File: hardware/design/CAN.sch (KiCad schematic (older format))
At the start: 3 parts, among them IC1 MAX3051EKA+T

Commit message: Six-phase power stage.
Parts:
- renumbered C401 to Ccan1, R401 to Rcan1
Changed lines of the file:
@@
 $Descr A4 11693 8268
 encoding utf-8
-Sheet 2 6
+Sheet 2 12
 Title "CAN BUS transceiver"
 Date "2015-08-27"
@@
 $EndDescr
 $Comp
-L C-RESCUE-BLDC_4 C401
+L C-RESCUE-BLDC_4 Ccan1
 U 1 1 53F59FA3
 P 6950 2850
-F 0 "C401" H 7065 2889 40  0000 L CNN
+F 0 "Ccan1" H 7065 2889 40  0000 L CNN
 F 1 "2.2u" H 7065 2811 40  0000 L CNN
 F 2 "Capacitors_SMD:C_0603" H 6988 2700 30  0001 C CNN
@@
 CAN_TX
 $Comp
-L R-RESCUE-BLDC_4 R401
+L R-RESCUE-BLDC_4 Rcan1
 U 1 1 540030A8
 P 5250 3650
-F 0 "R401" V 5330 3650 40  0000 C CNN
-F 1 "NI" V 5257 3651 40  0000 C CNN
+F 0 "Rcan1" H 5321 3689 40  0000 L CNN
+F 1 "NI" H 5321 3611 40  0000 L CNN
 F 2 "Resistors_SMD:R_0603_HandSoldering" V 5180 3650 30  0001 C CNN
 F 3 "" H 5250 3650 30  0000 C CNN

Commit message: Some more routing...
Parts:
- removed IC1: MAX3051EKA+T, Housings_SOT_User:SOT-23-8, symbol MAX3051EKA+T
- added Ccan2: 2.2u, Capacitors_SMD:C_0603, symbol C
- added U2: ISO1050, CRF1:PDSO-G8, symbol ISO1050
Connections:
- net labels added: GND2, VCC2
- wire segments 12 -> 18
- no-connect marks 1 -> 0
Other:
- moved on the sheet: Ccan1, Rcan1
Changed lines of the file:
@@
 L C-RESCUE-BLDC_4 Ccan1
 U 1 1 53F59FA3
-P 6950 2850
-F 0 "Ccan1" H 7065 2889 40  0000 L CNN
-F 1 "2.2u" H 7065 2811 40  0000 L CNN
-F 2 "Capacitors_SMD:C_0603" H 6988 2700 30  0001 C CNN
-F 3 "" H 6950 2850 60  0000 C CNN
-	1    6950 2850
+P 9550 3250
+F 0 "Ccan1" H 9665 3289 40  0000 L CNN
+F 1 "2.2u" H 9665 3211 40  0000 L CNN
+F 2 "Capacitors_SMD:C_0603" H 9588 3100 30  0001 C CNN
+F 3 "" H 9550 3250 60  0000 C CNN
+	1    9550 3250
 	1    0    0    -1
 $EndComp
@@
 EndData
 $EndBitmap
-Text HLabel 6700 3450 2    60   Output ~ 0
+Text HLabel 8750 3200 2    60   Output ~ 0
 CAN_RX
-Text HLabel 6700 3550 2    60   Input ~ 0
+Text HLabel 8750 3300 2    60   Input ~ 0
 CAN_TX
 $Comp
 L R-RESCUE-BLDC_4 Rcan1
 U 1 1 540030A8
-P 5250 3650
-F 0 "Rcan1" H 5321 3689 40  0000 L CNN
-F 1 "NI" H 5321 3611 40  0000 L CNN
-F 2 "Resistors_SMD:R_0603_HandSoldering" V 5180 3650 30  0001 C CNN
-F 3 "" H 5250 3650 30  0000 C CNN
-	1    5250 3650
+P 7000 3250
+F 0 "Rcan1" H 7071 3289 40  0000 L CNN
+F 1 "NI" H 7071 3211 40  0000 L CNN
+F 2 "Resistors_SMD:R_0603_HandSoldering" V 6930 3250 30  0001 C CNN
+F 3 "" H 7000 3250 30  0000 C CNN
+	1    7000 3250
 	1    0    0    -1
 $EndComp
-Text HLabel 5000 3400 0    60   Input ~ 0
+Text HLabel 6650 3000 0    60   BiDi ~ 0
 CANH
-Text HLabel 5000 3900 0    60   Input ~ 0
+Text HLabel 6650 3500 0    60   BiDi ~ 0
 CANL
-Wire Wire Line
-	5500 3900 5000 3900
-Connection ~ 5250 3900
-Wire Wire Line
-	5500 3400 5000 3400
-Connection ~ 5250 3400
 Text Notes 3450 2000 0    60   ~ 0
 TODO: Bus protection
 $Comp
-L GND #PWR13
+L GND #PWR013
 U 1 1 55E64902
-P 6250 4200
-F 0 "#PWR13" H 6250 3950 50  0001 C CNN
-F 1 "GND" H 6250 4050 50  0000 C CNN
-F 2 "" H 6250 4200 60  0000 C CNN
-F 3 "" H 6250 4200 60  0000 C CNN
-	1    6250 4200
+P 9050 3650
+F 0 "#PWR013" H 9050 3400 50  0001 C CNN
+F 1 "GND" H 9050 3500 50  0000 C CNN
+F 2 "" H 9050 3650 60  0000 C CNN
+F 3 "" H 9050 3650 60  0000 C CNN
+	1    9050 3650
 	1    0    0    -1
 $EndComp
 $Comp
-L GND #PWR15
-U 1 1 55E749EE
-P 6950 3050
-F 0 "#PWR15" H 6950 2800 50  0001 C CNN
-F 1 "GND" H 6950 2900 50  0000 C CNN
-F 2 "" H 6950 3050 60  0000 C CNN
-F 3 "" H 6950 3050 60  0000 C CNN
-	1    6950 3050
+L +3.3V #PWR014
+U 1 1 56AE4CAB
+P 9050 2900
+F 0 "#PWR014" H 9050 2750 50  0001 C CNN
+F 1 "+3.3V" H 9068 3074 50  0000 C CNN
+F 2 "" H 9050 2900 50  0000 C CNN
+F 3 "" H 9050 2900 50  0000 C CNN
+	1    9050 2900
 	1    0    0    -1
 $EndComp
 $Comp
-L MAX3051EKA+T IC1
-U 1 1 56AE48D1
-P 6250 3650
-F 0 "IC1" H 6250 4278 40  0000 C CNN
-F 1 "MAX3051EKA+T" H 6250 4200 40  0000 C CNN
-F 2 "Housings_SOT_User:SOT-23-8" H 6250 4126 35  0000 C CIN
-F 3 "" H 6250 3650 60  0000 C CNN
-	1    6250 3650
+L ISO1050 U2
+U 1 1 56DB0D06
+P 8150 3250
+F 0 "U2" H 8150 3793 60  0000 C CNN
+F 1 "ISO1050" H 8150 3687 60  0000 C CNN
+F 2 "CRF1:PDSO-G8" H 8150 3581 60  0000 C CNN
+F 3 "" H 8150 3250 60  0000 C CNN
+	1    8150 3250
 	-1   0    0    -1
 $EndComp
 Wire Wire Line
-	6250 4200 6250 4050
-Wire Wire Line
-	6700 3850 6700 4150
-Wire Wire Line
-	6700 4150 6250 4150
-Connection ~ 6250 4150
-Wire Wire Line
-	5500 3400 5500 3550
-Wire Wire Line
-	5500 3550 5800 3550
-Wire Wire Line
-	5500 3900 5500 3750
-Wire Wire Line
-	5500 3750 5800 3750
+	8750 2900 9550 2900
+Wire Wire Line
+	8750 2900 8750 3100
+Wire Wire Line
+	9550 2900 9550 3050
+Connection ~ 9050 2900
+Wire Wire Line
+	8750 3400 8750 3650
+Wire Wire Line
+	8750 3650 9550 3650
+Wire Wire Line
+	9550 3650 9550 3450
+Connection ~ 9050 3650
+Wire Wire Line
+	7550 3200 7300 3200
+Wire Wire Line
+	7300 3200 7300 3000
+Wire Wire Line
+	7300 3000 6650 3000
+Wire Wire Line
+	7550 3300 7300 3300
+Wire Wire Line
+	7300 3300 7300 3500
+Wire Wire Line
+	7300 3500 6650 3500
+Connection ~ 7000 3000
+Connection ~ 7000 3500
+Text HLabel 5800 2650 0    60   Input ~ 0
+VCC2
+Text HLabel 5800 3650 0    60   Input ~ 0
+GND2
 $Comp
-L +3.3V #PWR14
-U 1 1 56AE4CAB
-P 6950 2500
-F 0 "#PWR14" H 6950 2350 50  0001 C CNN
-F 1 "+3.3V" H 6968 2674 50  0000 C CNN
-F 2 "" H 6950 2500 50  0000 C CNN
-F 3 "" H 6950 2500 50  0000 C CNN
-	1    6950 2500
+L C Ccan2
+U 1 1 56DB9D5F
+P 5900 3150
+F 0 "Ccan2" H 6015 3242 50  0000 L CNN
+F 1 "2.2u" H 6015 3150 50  0000 L CNN
+F 2 "Capacitors_SMD:C_0603" H 6015 3058 50  0000 L CNN
+F 3 "" H 5900 3150 50  0000 C CNN
+	1    5900 3150
 	1    0    0    -1
 $EndComp
 Wire Wire Line
-	6950 2650 6950 2500
-Wire Wire Line
-	6250 3250 6250 2600
-Wire Wire Line
-	6250 2600 6950 2600
-Connection ~ 6950 2600
-NoConn ~ 6700 3700
+	5800 2650 7550 2650
+Wire Wire Line
+	7550 2650 7550 3100
+Wire Wire Line
+	5800 3650 7550 3650
+Wire Wire Line
+	7550 3650 7550 3400
+Wire Wire Line
+	5900 3000 5900 2650
+Connection ~ 5900 2650
+Wire Wire Line
+	5900 3300 5900 3650
+Connection ~ 5900 3650
 $EndSCHEMATC

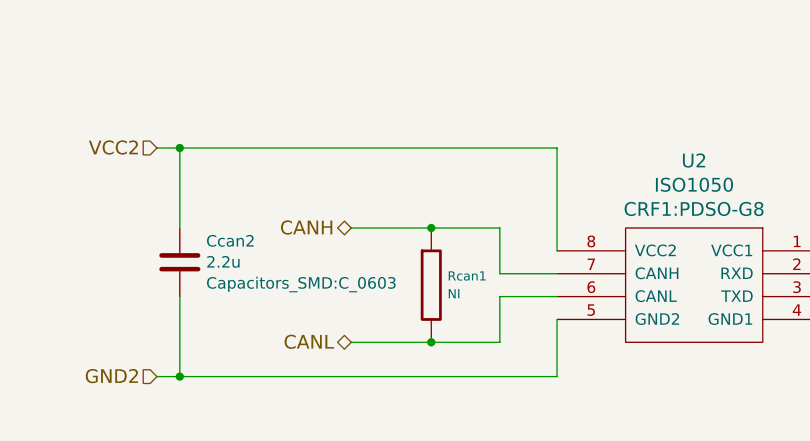
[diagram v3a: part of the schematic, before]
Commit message: Changed pin for LED3
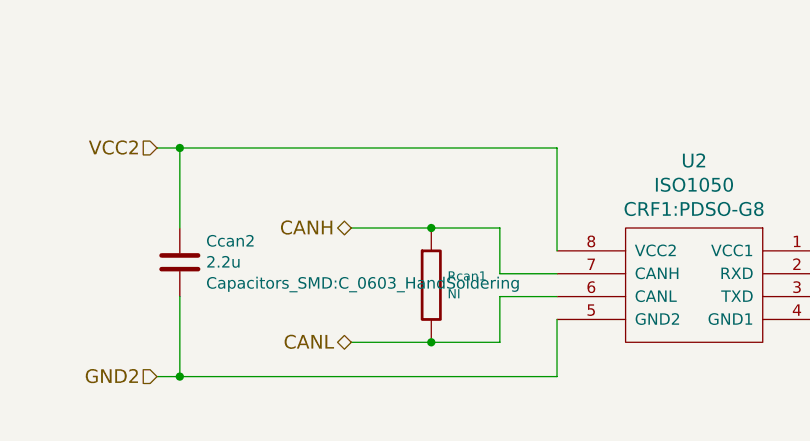
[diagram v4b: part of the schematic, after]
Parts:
- Ccan2: footprint Capacitors_SMD:C_0603 -> Capacitors_SMD:C_0603_HandSoldering
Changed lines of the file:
@@
 	1    0    0    -1
-$EndComp
-$Comp
-L ISO1050 U2
-U 1 1 56DB0D06
-P 8150 3250
-F 0 "U2" H 8150 3793 60  0000 C CNN
-F 1 "ISO1050" H 8150 3687 60  0000 C CNN
-F 2 "CRF1:PDSO-G8" H 8150 3581 60  0000 C CNN
-F 3 "" H 8150 3250 60  0000 C CNN
-	1    8150 3250
-	-1   0    0    -1
 $EndComp
 Wire Wire Line
@@
 F 0 "Ccan2" H 6015 3242 50  0000 L CNN
 F 1 "2.2u" H 6015 3150 50  0000 L CNN
-F 2 "Capacitors_SMD:C_0603" H 6015 3058 50  0000 L CNN
+F 2 "Capacitors_SMD:C_0603_HandSoldering" H 6015 3058 50  0000 L CNN
 F 3 "" H 5900 3150 50  0000 C CNN
 	1    5900 3150
@@
 	5900 3300 5900 3650
 Connection ~ 5900 3650
+$Comp
+L ISO1050 U2
+U 1 1 56DB0D06
+P 8150 3250
+F 0 "U2" H 8150 3793 60  0000 C CNN
+F 1 "ISO1050" H 8150 3687 60  0000 C CNN
+F 2 "CRF1:PDSO-G8" H 8150 3581 60  0000 C CNN
+F 3 "" H 8150 3250 60  0000 C CNN
+	1    8150 3250
+	-1   0    0    -1
+$EndComp
 $EndSCHEMATC
